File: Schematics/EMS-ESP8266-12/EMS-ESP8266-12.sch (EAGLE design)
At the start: 43 parts, among them IC1 LM393N, T1 BC547B, T2 BC547B

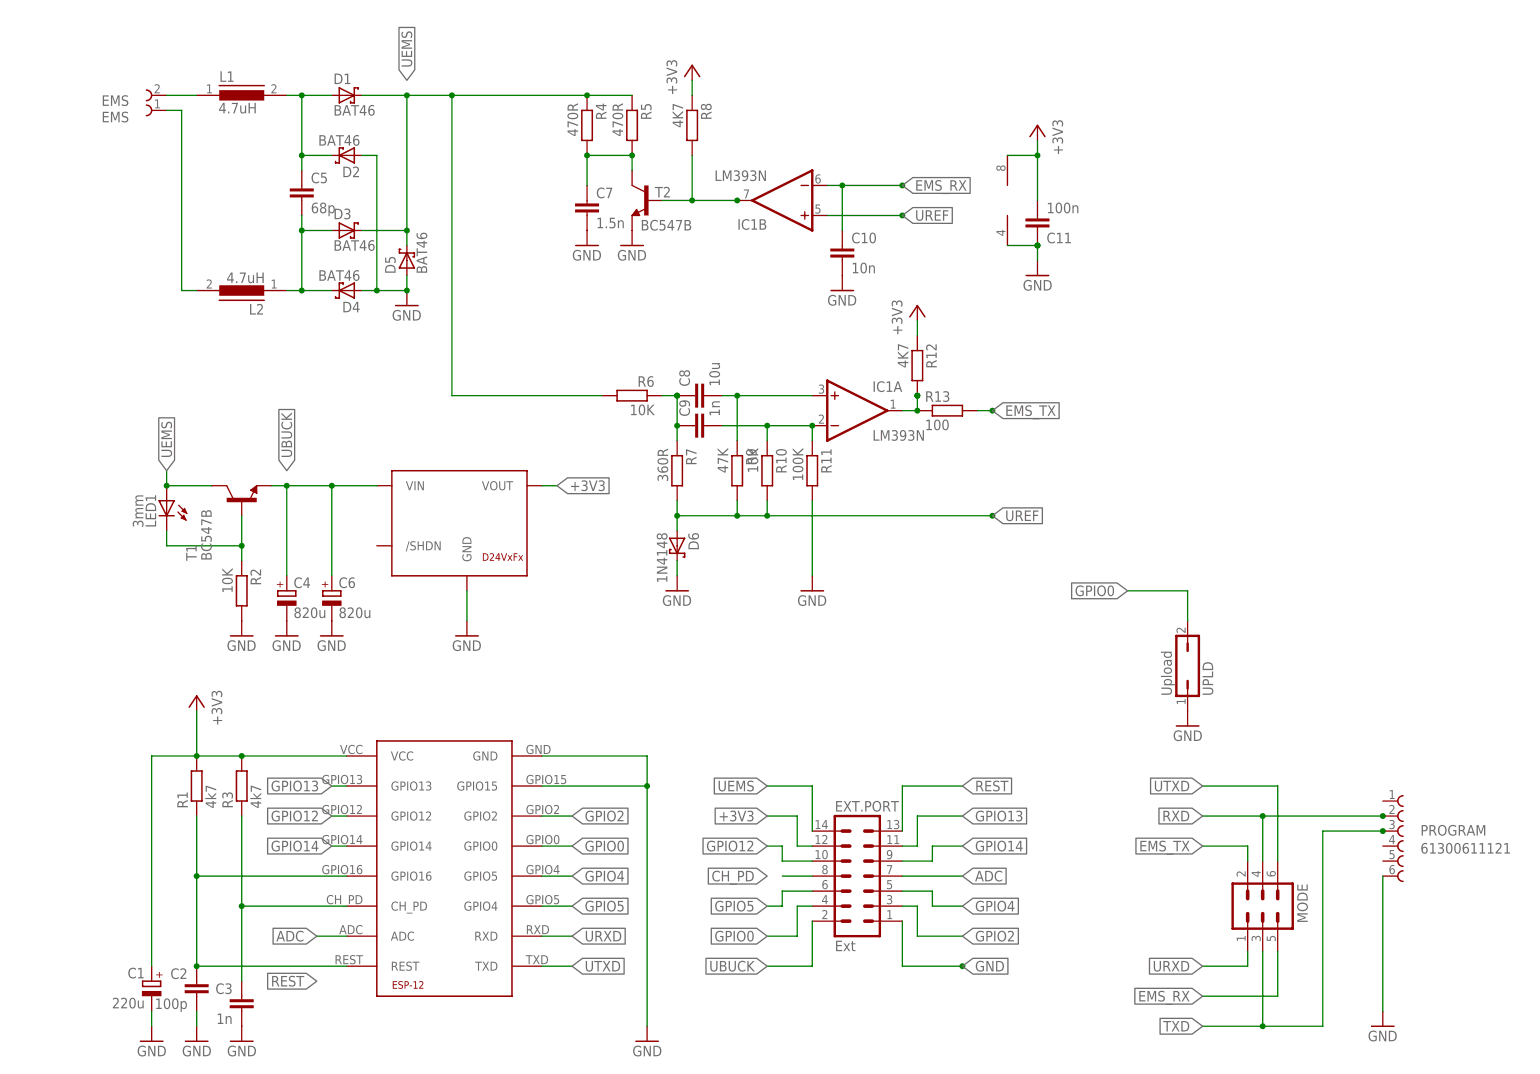
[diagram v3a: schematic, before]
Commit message: Board Rev 1.0b - Ext. Port auf 16pin erweitert - GPIO15 auf Ext. Port gelegt - erfordert im Normalbetrieb einen  Jumper zw. Ext.Port, Pin 3-4 - Dummy Solder Jumper für Buck-Konverter /SHDN
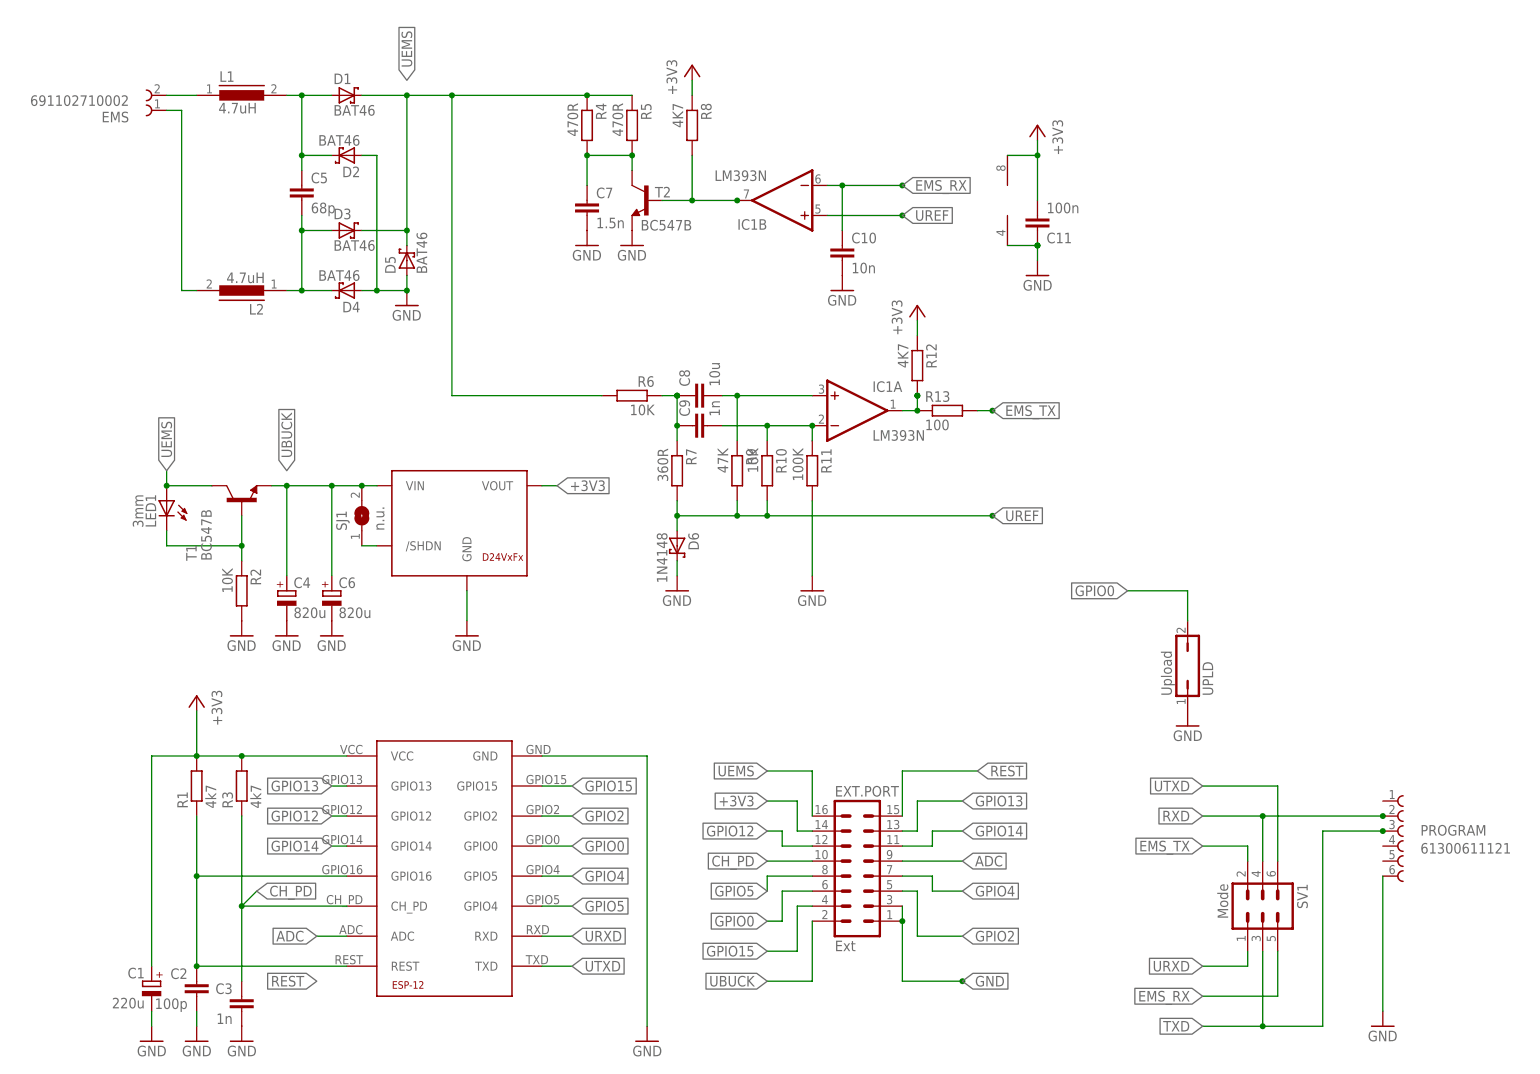
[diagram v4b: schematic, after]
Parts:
- added SJ1: n.u., jumper:SJ
- EMS: value EMS -> 691102710002
- EXT.PORT: device con-lstb:MA07-2 -> con-lstb:MA08-2
- SV1: value (none) -> Mode
- renumbered MODE to SV1
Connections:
- new net N$3: MOD1./SHDN, SJ1.1
- net +3V3: now also EXT.PORT.14; no longer EXT.PORT.12
- net ADC: now also EXT.PORT.9; no longer EXT.PORT.7
- net CH_PD: now also EXT.PORT.10; no longer EXT.PORT.8
- net GND: now also ESP1.GND, EXT.PORT.3
- net GPIO0: now also EXT.PORT.6; no longer EXT.PORT.4
- net GPIO12: now also EXT.PORT.12; no longer EXT.PORT.10
- net GPIO13: now also EXT.PORT.13; no longer EXT.PORT.11
- net GPIO14: now also EXT.PORT.11; no longer EXT.PORT.9
- net GPIO15: now also EXT.PORT.4; no longer ESP1.GND
- net GPIO2: now also EXT.PORT.5; no longer EXT.PORT.3
- net GPIO4: now also EXT.PORT.7; no longer EXT.PORT.5
- net GPIO5: now also EXT.PORT.8; no longer EXT.PORT.6
- net REST: now also EXT.PORT.15; no longer EXT.PORT.13
- net UBUCK: now also SJ1.2
- net UEMS: now also EXT.PORT.16; no longer EXT.PORT.14

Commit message: work in progress
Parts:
- C1: CONRAD VF 220/6,3 P-D -> (none); REICHELT (none) -> VF 220/6,3 P-D
- C10: REICHELT (none) -> X7R-2,5 10N
- C11: REICHELT (none) -> X7R-2,5 100N
- C2: REICHELT (none) -> KERKO 100P
- C3: REICHELT (none) -> X7R-2,5 1,0N
- C4, C6: CONRAD VF 820/16 P-G -> (none); REICHELT (none) -> VF 820/16 P-G
- C5: CONRAD 457221-62 -> (none); REICHELT (none) -> KERKO 68P
- C7: REICHELT (none) -> X7R-2,5 1,5N
- C9: CONRAD 453005-62 -> (none); REICHELT (none) -> X7R-2,5 1,0N
- D1, D2, D3, D4, D5: CONRAD 153087-62 -> (none); REICHELT (none) -> BAT 46
- D6: CONRAD 162280-62 -> (none); REICHELT (none) -> 1N 4148
- EMS: REICHELT (none) -> AKL 055-02
- ESP1: AI-THINKER (none) -> ESP-12
- EXT.PORT: REICHELT (none) -> MPE 087-2-016
- IC1: REICHELT (none) -> LM 393 DIP
- L1, L2: CONRAD 440391-62 -> (none); REICHELT (none) -> SMCC 4,70µ
- LED1: REICHELT (none) -> LED 3MM ST RT
- MOD1: POLOLU (none) -> D24V3F3
- PROGRAM: REICHELT (none) -> MPE 087-1-006
- R1, R12, R3, R8: REICHELT (none) -> METALL 4,70K
- R10, R2, R6: REICHELT (none) -> METALL 10,0K
- R11: REICHELT (none) -> METALL 100K
- R13: REICHELT (none) -> METALL 100
- R4, R5: REICHELT (none) -> METALL 470
- R7: REICHELT (none) -> METALL 360
- R9: REICHELT (none) -> METALL 47,0K
- SV1: REICHELT (none) -> MPE 087-2-006
- T1, T2: REICHELT (none) -> BC 547B
- UPLD: REICHELT (none) -> MPE 087-1-002
